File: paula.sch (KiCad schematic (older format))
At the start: 79 parts, among them CN200 DB9P RIGHT(1), CN201 DB9P LEFT(0), CN204 RIGHT AUDIO, CN205 LEFT AUDIO, J200 Conn_01x03_Male, Q200 MPF102, Q201 MPF102, Q202 2N3906, U200 PAULA, U202 74LS157, U204 LF347

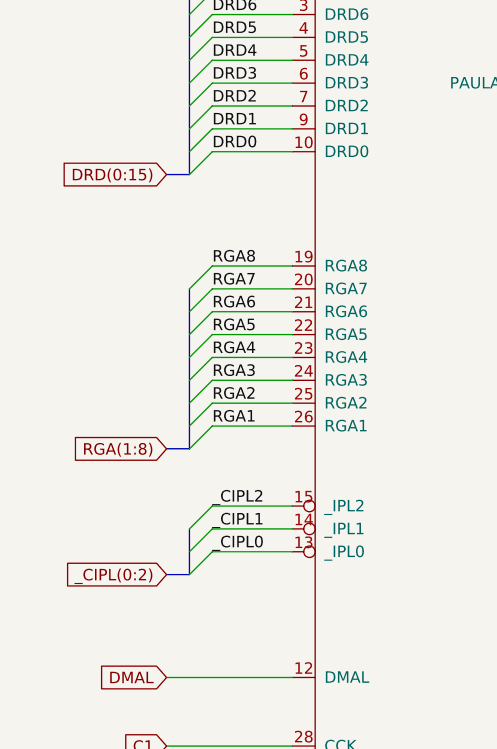
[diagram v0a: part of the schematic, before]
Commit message: Rename bus with correct syntax
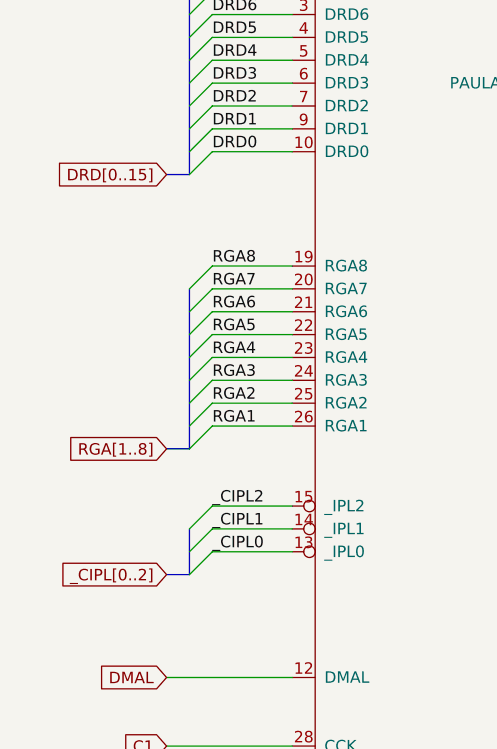
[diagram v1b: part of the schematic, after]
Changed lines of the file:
@@
-EESchema Schematic File Version 4
+EESchema Schematic File Version 5
 LIBS:amiga2000-cache
 EELAYER 29 0
@@
 	1300 3300 1200 3300
 Text GLabel 1200 3300 0    50   Input ~ 0
-DRD(0:15)
+DRD[0..15]
 Text Label 1400 3700 0    50   ~ 0
 RGA8
@@
 	1300 4500 1400 4400
 Text GLabel 1200 4500 0    50   Input ~ 0
-RGA(1:8)
+RGA[1..8]
 Wire Bus Line
 	1200 4500 1300 4500
@@
 	1400 4750 1750 4750
 Text GLabel 1200 5050 0    50   Input ~ 0
-_CIPL(0:2)
+_CIPL[0..2]
 Entry Wire Line
 	1300 4850 1400 4750

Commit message: squeak
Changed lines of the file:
@@
 Wire Bus Line
 	1300 1800 1300 3300
+$Comp
+L power:PWR_FLAG #FLG01
+U 1 1 5D60601F
+P 1150 750
+F 0 "#FLG01" H 1150 825 50  0001 C CNN
+F 1 "PWR_FLAG" H 1150 923 50  0000 C CNN
+F 2 "" H 1150 750 50  0001 C CNN
+F 3 "~" H 1150 750 50  0001 C CNN
+	1    1150 750
+	1    0    0    -1
+$EndComp
+Text GLabel 1150 750  3    50   Input ~ 0
++AUD
+$Comp
+L power:PWR_FLAG #FLG02
+U 1 1 5D91D9C8
+P 10850 8000
+F 0 "#FLG02" H 10850 8075 50  0001 C CNN
+F 1 "PWR_FLAG" H 10850 8173 50  0000 C CNN
+F 2 "" H 10850 8000 50  0001 C CNN
+F 3 "~" H 10850 8000 50  0001 C CNN
+	1    10850 8000
+	1    0    0    -1
+$EndComp
+$Comp
+L power:PWR_FLAG #FLG03
+U 1 1 5D91DF6A
+P 10850 9000
+F 0 "#FLG03" H 10850 9075 50  0001 C CNN
+F 1 "PWR_FLAG" H 10850 9173 50  0000 C CNN
+F 2 "" H 10850 9000 50  0001 C CNN
+F 3 "~" H 10850 9000 50  0001 C CNN
+	1    10850 9000
+	-1   0    0    1
+$EndComp
 $EndSCHEMATC

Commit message: Review started; oopsie whoopsie
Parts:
- removed FB201, FB202, FB203, FB204, FB205, FB206, FB207, FB208, FB209, FB210, FB211, FB212, FB213, FB214: Ferrite_Bead_Small, symbol Device:Ferrite_Bead_Small
- added EMI230, EMI231, EMI232, EMI233, EMI234, EMI235, EMI236, EMI237, EMI238, EMI239, EMI240, EMI241, EMI242, EMI243: C_Feedthrough, symbol Device:C_Feedthrough
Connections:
- net +AV: now also U204.4 (V+); no longer U204.11 (V-)
- net -AV: now also U204.11 (V-); no longer U204.4 (V+)
- net BACK: now also EMI231.3, EMI235.3
- net FIRE: now also EMI238.1, EMI241.1
- net FORWARD: now also EMI230.3, EMI234.3
- net GND: now also EMI230.2, EMI231.2, EMI232.2, EMI233.2, EMI234.2, EMI235.2, EMI236.2, EMI237.2, EMI238.2, EMI239.2, EMI240.2, EMI241.2, EMI242.2, EMI243.2
- net LEFT: now also EMI232.3, EMI236.3
- net POTX: now also EMI240.1, EMI243.1
- net POTY: now also EMI239.1, EMI242.1
- net RIGHT: now also EMI233.3, EMI237.3
- net _FIR0: now also J200.3 (Pin_3), EMI241.3; no longer J200.1 (Pin_1)
- net _FIR1: now also J200.1 (Pin_1), EMI238.3; no longer J200.3 (Pin_3)
- net at C210.1, U200.32 (P0X): now also EMI243.3
- net at C211.1, U200.33 (P0Y): now also EMI242.3
- net at C212.1, U200.35 (P1X): now also EMI240.3
- net at C213.1, U200.36 (P1Y): now also EMI239.3
- net at RP200.7 (R6), U202.10 (I1c): now also EMI236.1
- net at RP200.6 (R5), U202.11 (I0c): now also EMI234.1
- net at RP200.9 (R8), U202.13 (I1d): now also EMI237.1
- net at RP200.8 (R7), U202.14 (I0d): now also EMI235.1
- net at RP200.2 (R1), U202.2 (I0a): now also EMI230.1
- net at RP200.3 (R2), U202.3 (I1a): now also EMI232.1
- net at RP200.4 (R3), U202.5 (I0b): now also EMI231.1
- net at RP200.5 (R4), U202.6 (I1b): now also EMI233.1
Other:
- note added: "2-1 A500 STD\n\n2-3 A1000 OLD"
- note removed: "2-3 A500\n\n2-1 A1000"
- moved on the sheet: C202, C218, C220, C221, C222, C223, C900, C901, CN200, CN201, F1, FB215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

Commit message: Add gender to connectors
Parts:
- CN200, CN201: symbol Connector:DB9_Female -> Connector:DB9_Male_MountingHoles; Gender (none) -> Male
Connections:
- net GND: now also CN200.0 (PAD), CN201.0 (PAD)
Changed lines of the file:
@@
 $EndComp
 $Comp
-L Connector:DB9_Female CN200
+L Connector:DB9_Male_MountingHoles CN200
 U 1 1 5CF14CAD
 P 8450 7700
@@
 F 2 "" H 8450 7700 50  0001 C CNN
 F 3 " ~" H 8450 7700 50  0001 C CNN
+F 4 "Male" H 8450 7700 50  0001 C CNN "Gender"
 	1    8450 7700
-	1    0    0    -1
+	1    0    0    1
 $EndComp
 $Comp
@@
 POTX
 $Comp
-L Connector:DB9_Female CN201
+L Connector:DB9_Male_MountingHoles CN201
 U 1 1 5CF88629
 P 8500 9900
@@
 F 2 "" H 8500 9900 50  0001 C CNN
 F 3 " ~" H 8500 9900 50  0001 C CNN
+F 4 "Male" H 8500 9900 50  0001 C CNN "Gender"
 	1    8500 9900
-	1    0    0    -1
+	1    0    0    1
 $EndComp
 Text Label 7800 9500 0    50   ~ 0
@@
 Wire Wire Line
 	7650 10000 7650 10300
+Connection ~ 7650 10300
 Wire Bus Line
 	1300 4850 1300 5050
@@
 Wire Bus Line
 	1300 1800 1300 3300
-Connection ~ 7650 10300
+$Comp
+L power:GND #PWR?
+U 1 1 5D8F333D
+P 8450 7100
+F 0 "#PWR?" H 8450 6850 50  0001 C CNN
+F 1 "GND" H 8455 6927 50  0000 C CNN
+F 2 "" H 8450 7100 50  0001 C CNN
+F 3 "" H 8450 7100 50  0001 C CNN
+	1    8450 7100
+	0    -1   -1   0
+$EndComp
+$Comp
+L power:GND #PWR?
+U 1 1 5D8F3978
+P 8500 9300
+F 0 "#PWR?" H 8500 9050 50  0001 C CNN
+F 1 "GND" H 8505 9127 50  0000 C CNN
+F 2 "" H 8500 9300 50  0001 C CNN
+F 3 "" H 8500 9300 50  0001 C CNN
+	1    8500 9300
+	0    -1   -1   0
+$EndComp
 $EndSCHEMATC
